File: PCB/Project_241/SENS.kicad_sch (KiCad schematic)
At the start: 14 parts, among them J2 Wind_Hall, J5 Rain_Hall, U3 LM393, U5 HDC1080

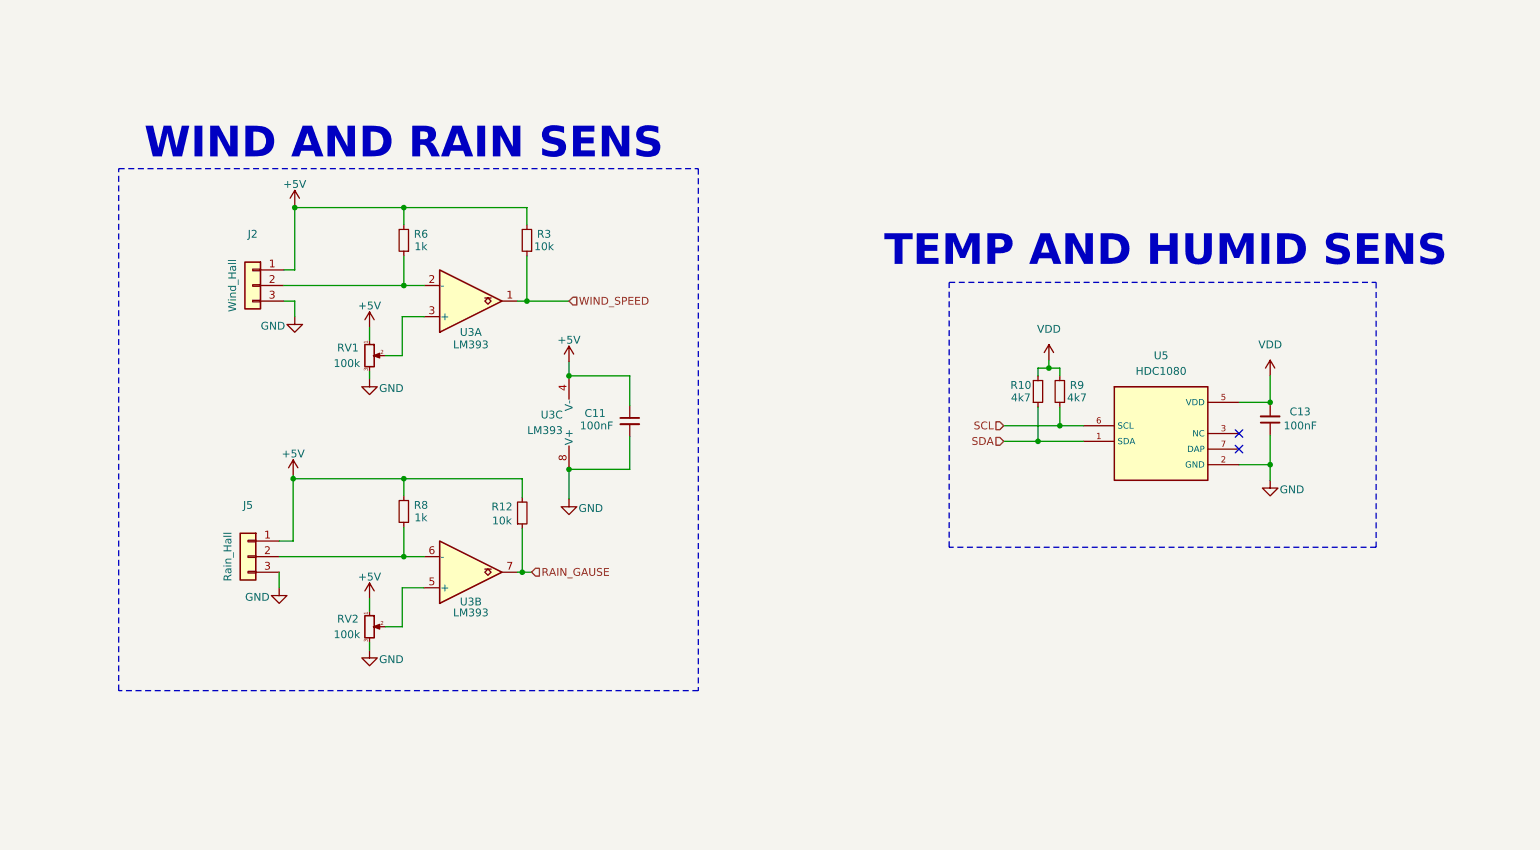
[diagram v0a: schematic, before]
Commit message: update schematic
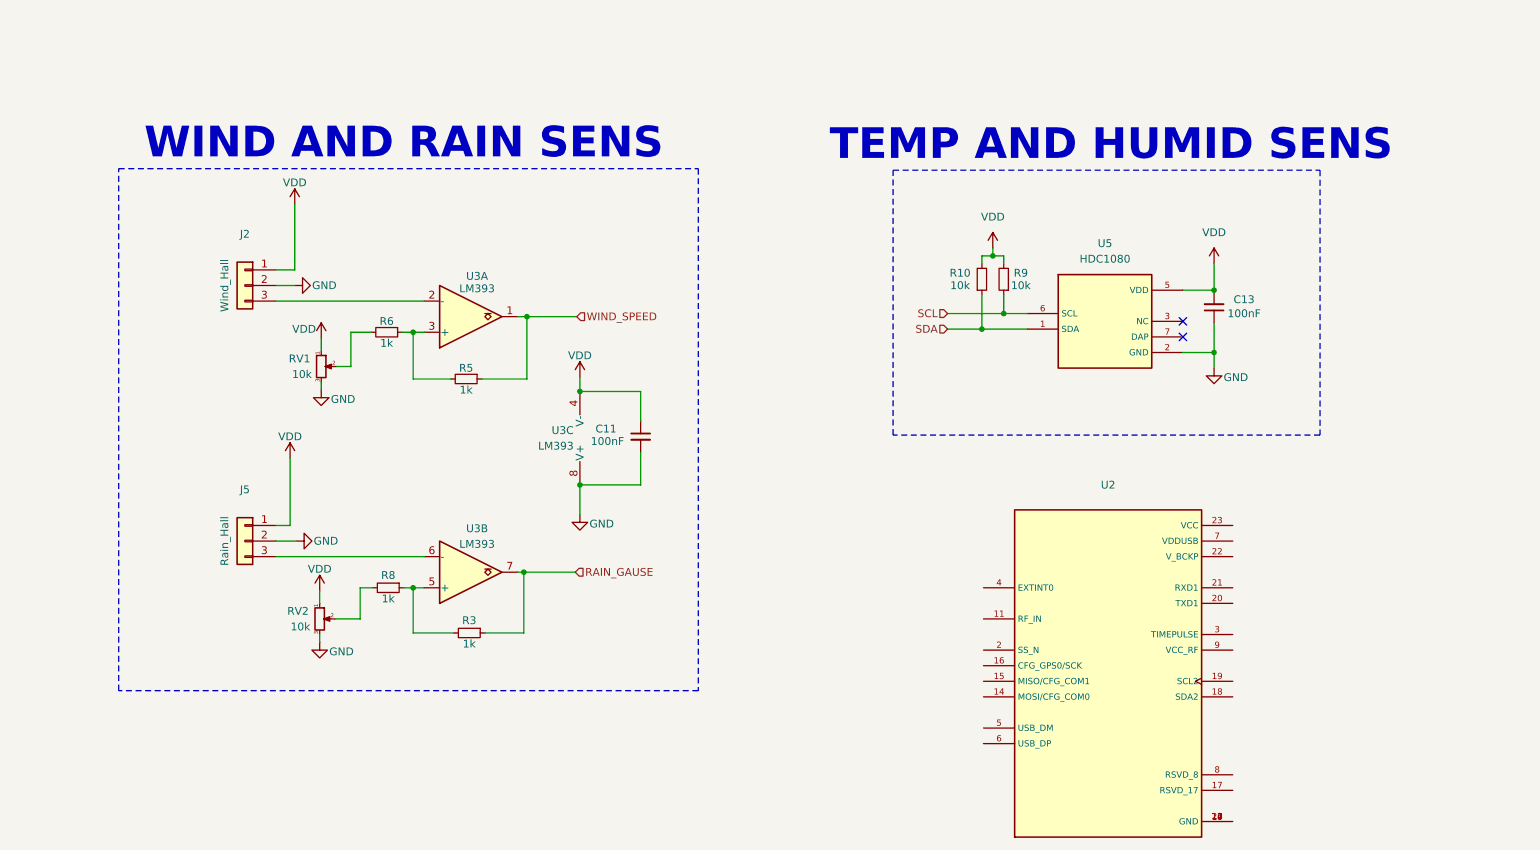
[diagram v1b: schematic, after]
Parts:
- removed R12: 10k, symbol Device:R_Small
- added R5: 1k, Resistor_SMD:R_0603_1608Metric, symbol Device:R_Small
- added U2: ~, project241_footprint:XCVR_NEO-6M-GPS, symbol project241_sym:NEO_6M
- C11, C13: footprint (none) -> Capacitor_SMD:C_0603_1608Metric
- J2, J5: footprint (none) -> IVSFootprint:XH_3P_2.54mm_Vertical
- R10, R9: value 4k7 -> 10k; footprint (none) -> Resistor_SMD:R_0603_1608Metric
- R3: value 10k -> 1k; footprint (none) -> Resistor_SMD:R_0603_1608Metric
- R6, R8: footprint (none) -> Resistor_SMD:R_0603_1608Metric
- RV1, RV2: value 100k -> 10k; footprint (none) -> Resistor_SMD:R_0603_1608Metric
- U3: footprint (none) -> Package_SO:SO-8_3.9x4.9mm_P1.27mm
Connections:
- net GND: now also J2.2 (Pin_2), J5.2 (Pin_2); no longer J2.3 (Pin_3), J5.3 (Pin_3)
- net RAIN_GAUSE: now also R3.1
- net VDD: now also C11.1, J2.1 (Pin_1), J5.1 (Pin_1), RV1.1, RV2.1, U3.4 (V-)
- net WIND_SPEED: now also R5.1; no longer R3.1
- net at U3.5 (+): now also R3.2, R8.1; no longer RV2.2
- net at U3.3 (+): now also R6.1, R5.2; no longer RV1.2
- removed net +5V: C11.1, J2.1 (Pin_1), J5.1 (Pin_1), R3.2, R6.2, R8.2, RV1.1, RV2.1, U3.4 (V-)
- new net: J5.3 (Pin_3), U3.6 (-)
- new net: R6.2, RV1.2
- new net: J2.3 (Pin_3), U3.2 (-)
- new net: R8.2, RV2.2
- new net: U2.10 (GND), U2.12 (GND), U2.13 (GND), U2.24 (GND)
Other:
- moved on the sheet: C11, C13, J2, J5, R10, R6, R8, R9, RV1, RV2, U3A, U3C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

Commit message: update gerber
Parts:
- removed R8: 1k, Resistor_SMD:R_0603_1608Metric, symbol Device:R_Small
- removed RV2: 10k, Resistor_SMD:R_0603_1608Metric, symbol Device:R_Potentiometer_Small
- removed U3: LM393, Package_SO:SO-8_3.9x4.9mm_P1.27mm, symbol Comparator:LM393
- added ANT1: IPEX_SMA, project241_footprint:ANT_SMA_3PIN, symbol project241_sym:IPEX_ANT
- added C14: 100nF, Capacitor_SMD:C_0603_1608Metric, symbol Device:C_Small
- added C15: 4.7uF, Capacitor_SMD:C_0603_1608Metric, symbol Device:C
- added C16: 100nF, Capacitor_SMD:C_0603_1608Metric, symbol Device:C
- added D2: RED_LED, LED_SMD:LED_0603_1608Metric, symbol Device:LED
- added L1: 27nH, Inductor_SMD:L_0603_1608Metric, symbol Device:L_Small
- added R12, R14, R15, R7: DNP, Resistor_SMD:R_0603_1608Metric, symbol Device:R_Small
- added R13, R18: 2k2, Resistor_SMD:R_0603_1608Metric, symbol Device:R_Small
- added R16: 1k, Resistor_SMD:R_0603_1608Metric, symbol Device:R_Small
- added R17: 15k, Resistor_SMD:R_0603_1608Metric, symbol Device:R_Small
- added R19: 22R, Resistor_SMD:R_0603_1608Metric, symbol Device:R_Small
- added RV3: 10k, project241_footprint:Poten_3PIN_SMD, symbol Device:R_Potentiometer_Small
- added U3, U6: LM358, IVSFootprint:SOIC-8, symbol Amplifier_Operational:LM358
- R3: value 1k -> 100R
- R5: value 1k -> 15k
- RV1: footprint Resistor_SMD:R_0603_1608Metric -> project241_footprint:Poten_3PIN_SMD
- U2: value ~ -> NEO 6M
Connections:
- net GND: now also U2.10 (GND), U2.12 (GND), U2.13 (GND), U2.24 (GND), ANT1.2 (GND), ANT1.3 (GND), C14.2, C15.1, C16.1, D2.1 (K), R12.2, R15.2, RV3.3, U3.4 (V-), U6.4 (V-)
- net RAIN_GAUSE: now also R17.1, R18.2, U3.1; no longer R3.1
- net VDD: now also U2.23 (VCC), C14.1, C15.2, C16.2, R13.1, R14.1, R18.1, R7.1, RV3.1, U3.8 (V+), U6.8 (V+)
- net WIND_SPEED: now also R13.2, U6.1
- net at R3.2: now also U2.3 (TIMEPULSE)
- net at J5.3 (Pin_3): now also U3.2 (-)
- net at R5.2, R6.1: now also U6.3 (+)
- net at R6.2: now also U6.6 (-), U6.7; no longer RV1.2
- net at J2.3 (Pin_3): now also U6.2 (-)
- net at U2.11 (RF_IN): now also ANT1.1 (FEED), L1.2
- net GPS_TX: now reaches U2.20 (TXD1)
- net GPS_RX: now reaches U2.21 (RXD1)
- net at U2.8 (RSVD_8): now also U2.9 (VCC_RF), R19.2
- new net: L1.1, R19.1
- new net: D2.2 (A), R3.1
- new net: R12.1, R7.2, RV1.2, U6.5 (+)
- new net: R16.1, R17.2, U3.3 (+)
- new net: R14.2, R15.1, RV3.2, U3.5 (+)
- new net: R16.2, U3.6 (-), U3.7
- no-connect marks 2 -> 15
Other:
- note added: "GPS"
- moved on the sheet: C11, C13, J2, J5, R10, R5, R6, R9, RV1, U5
